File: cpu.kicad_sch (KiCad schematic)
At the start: 10 parts, among them J2 CUI_UJC-HP-M-G-5-MSMT-TR

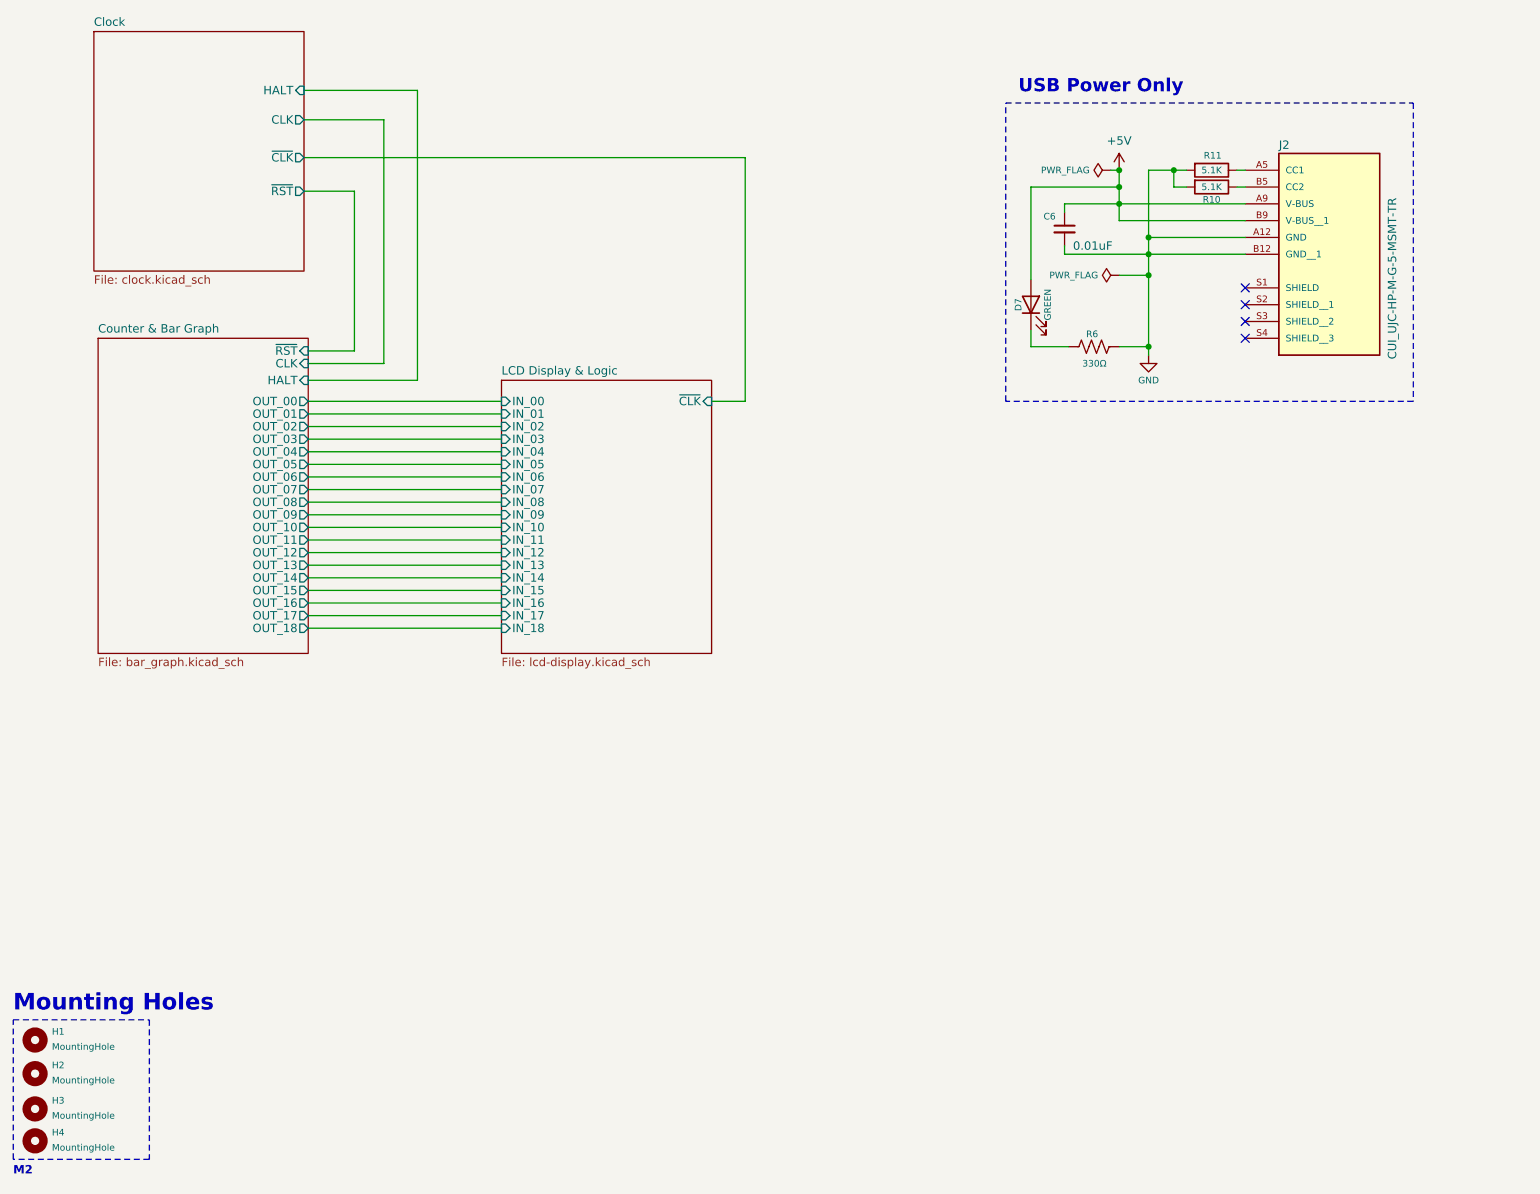
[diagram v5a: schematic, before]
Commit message: First KiCad v8 version.All ERC/DRC errors/warnings fixed - had to fix nets on left end of audio potentiometer so that they match. Weird.
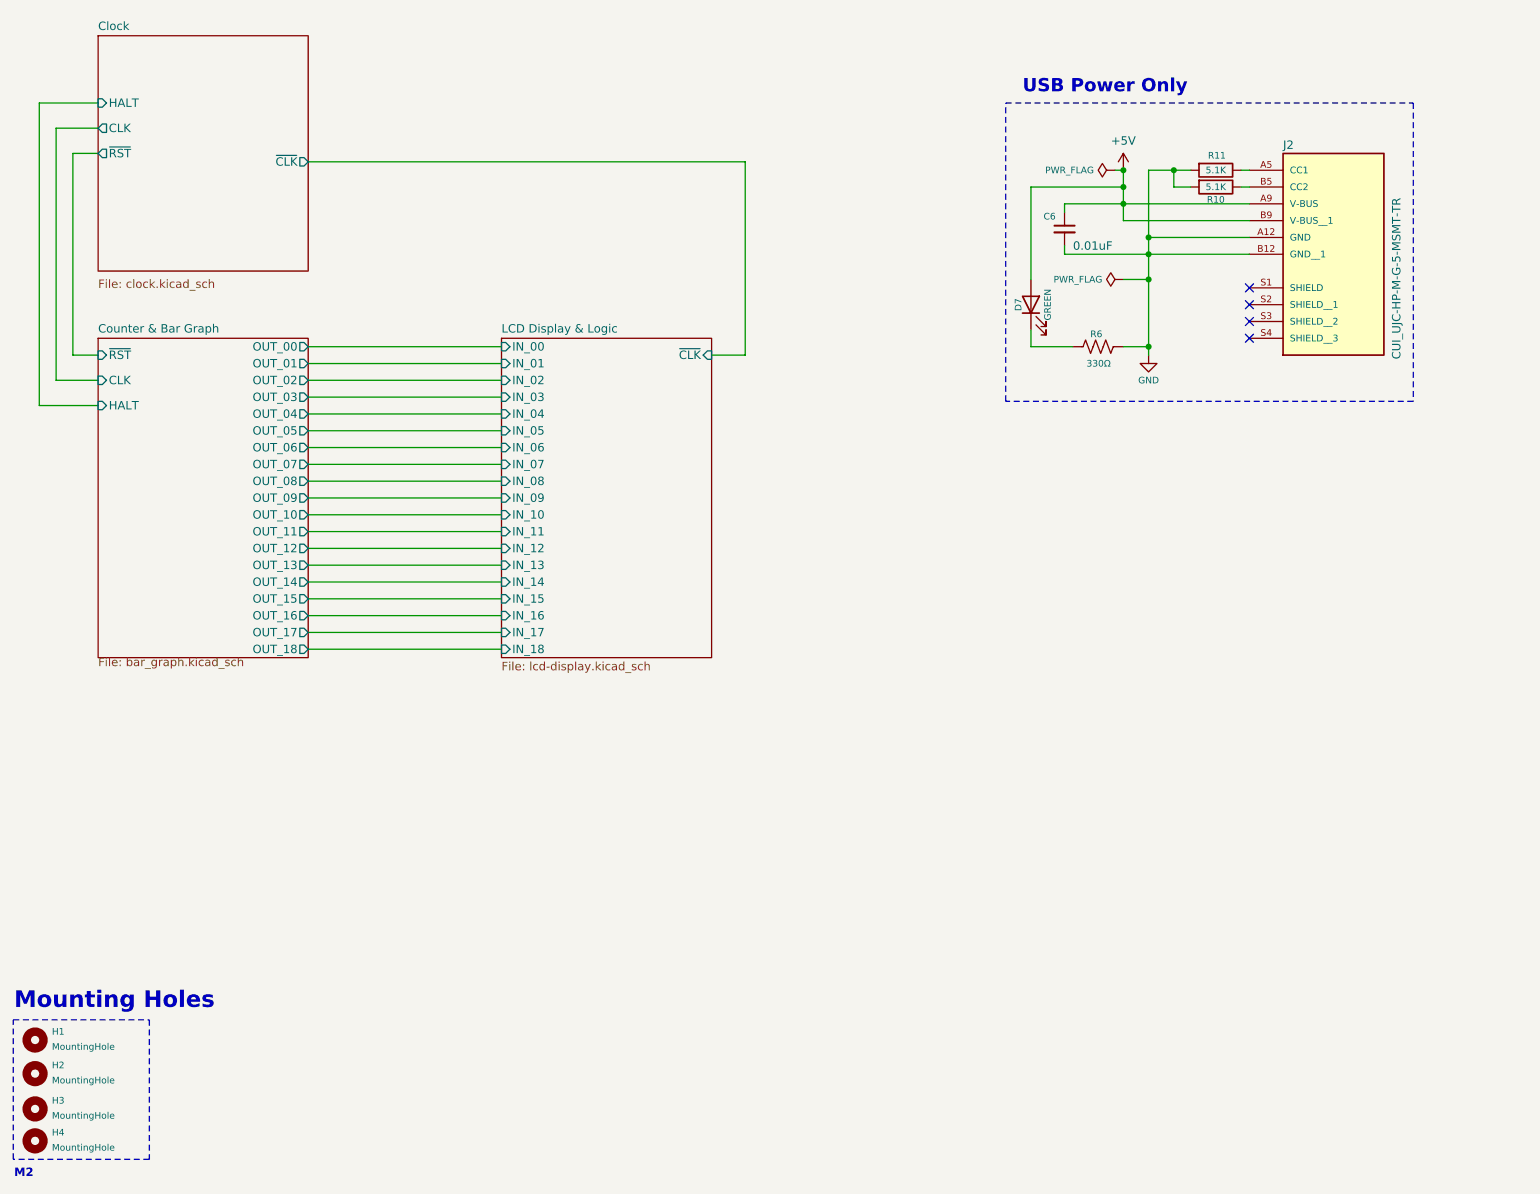
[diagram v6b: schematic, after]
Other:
- moved on the sheet: J2, R10, R11, R6
